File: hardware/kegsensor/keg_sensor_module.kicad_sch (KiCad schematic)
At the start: 7 parts, among them J1 Sensor_FL, J2 Sensor_FR, J3 Sensor_BR, J4 Sensor_BL, J5 HX711_LoadCell_Side, J6 HX711_Digital_Side, J7 RJ11_to_Hub

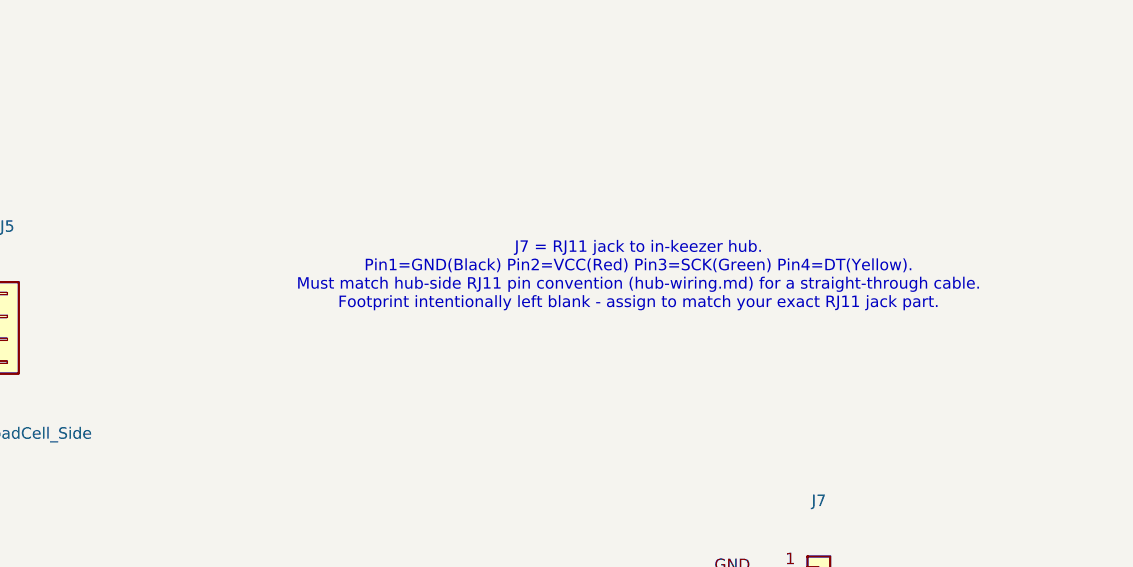
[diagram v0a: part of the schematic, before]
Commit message: Split hub-wiring.md and fix cross-references after the reorg
Split the old combined hub-wiring.md into hardware/kegsensor/wiring.md
(per-keg sensor wiring) and hardware/keghub/README.md (passive panel
wiring), along the KegSensor/KegHub boundary. Fixed hardcoded output
paths in generate_schematic.py/generate_pcb.py, the embedded doc
reference in the schematic's J7 annotation text, and all remaining
markdown/gitignore references to the old directory names.

Co-Authored-By: Claude Sonnet 5 <noreply@anthropic.com>
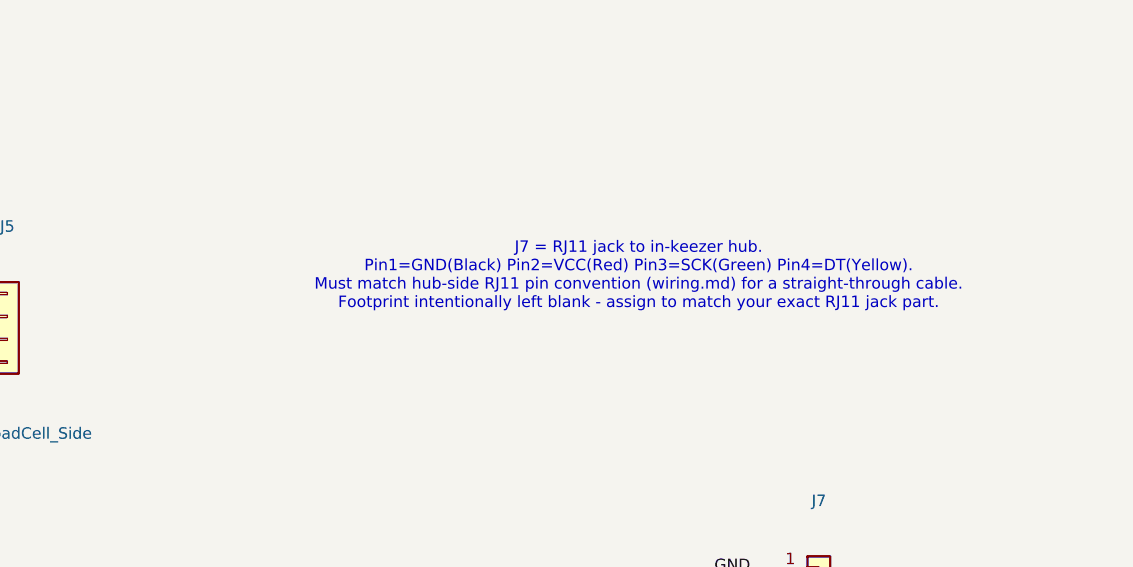
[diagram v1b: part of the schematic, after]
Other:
- note added: "J7 = RJ11 jack to in-keezer hub. Pin1=GND(Black) Pin2=VCC(Red) Pin3=SCK(Green) Pin4=DT(Yellow). Must match hub-side RJ11 pin convention (wiring.md) for a straight-through cable. Footprint intentionally left blank - assign to match your exact RJ11 jack part."
- note removed: "J7 = RJ11 jack to in-keezer hub. Pin1=GND(Black) Pin2=VCC(Red) Pin3=SCK(Green) Pin4=DT(Yellow). Must match hub-side RJ11 pin convention (hub-wiring.md) for a straight-through cable. Footprint intentionally left blank - assign to match your exact RJ11 jack part."
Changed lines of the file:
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@@
 		)
 	)
-	(text "J7 = RJ11 jack to in-keezer hub.\nPin1=GND(Black) Pin2=VCC(Red) Pin3=SCK(Green) Pin4=DT(Yellow).\nMust match hub-side RJ11 pin convention (hub-wiring.md) for a straight-through cable.\nFootprint intentionally left blank - assign to match your exact RJ11 jack part."
+	(text "J7 = RJ11 jack to in-keezer hub.\nPin1=GND(Black) Pin2=VCC(Red) Pin3=SCK(Green) Pin4=DT(Yellow).\nMust match hub-side RJ11 pin convention (wiring.md) for a straight-through cable.\nFootprint intentionally left blank - assign to match your exact RJ11 jack part."
 		(at 220 40 0)
 		(effects
